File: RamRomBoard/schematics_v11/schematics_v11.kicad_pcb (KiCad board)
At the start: 2 copper layers, 100 x 100 mm, 101 parts, among them J1 BUS, J10 Micro_SD_Card_Det2, J2 BUS, J3 VSEL, J5 Screw_Terminal_01x02, J6 USB_B_Micro, J7 STM32F401, J8 Dual LED Socket, J9 JTAG, SW1 033TBVSA, SW2 SW_Push, U1 74LVC125, U10 74AHC1G14, U11 IS61WV102416FBLL1T2, U12 IS61WV10248EDBLL-10TL, U13 74LVC595, U14 74LVC595, U15 SN74LVC245ANSR, U16 SN74LVC245ANSR, U17 74LVC595, U18 74HC165, U19 SN74LVC245ANSR, U2 AZ1117-3.3, U20 DS1314, U3 74LVC08AD, U4 DS1085, U5 74LVC1G32, U6 74AHC1G14, U7 74HC590, U8 74HC590, U9 74HC590

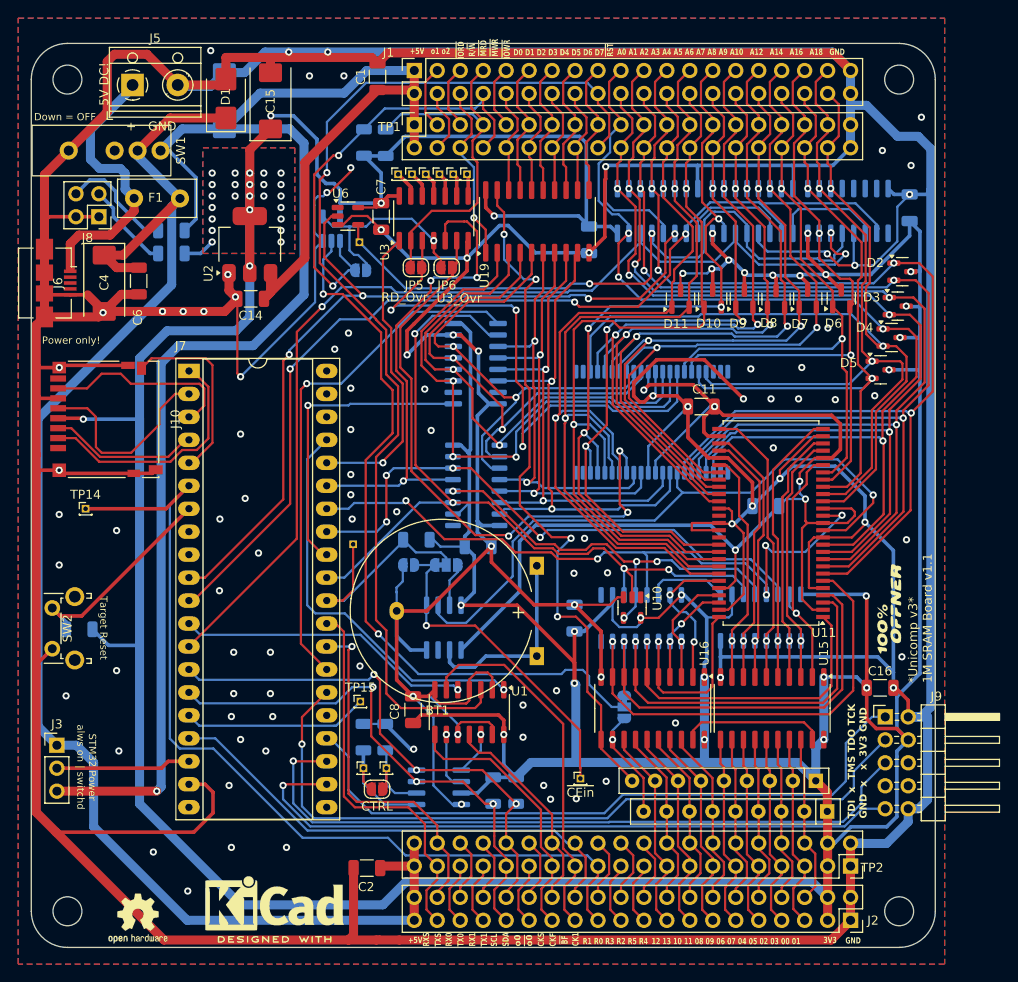
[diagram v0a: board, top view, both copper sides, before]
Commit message: new vhdl code
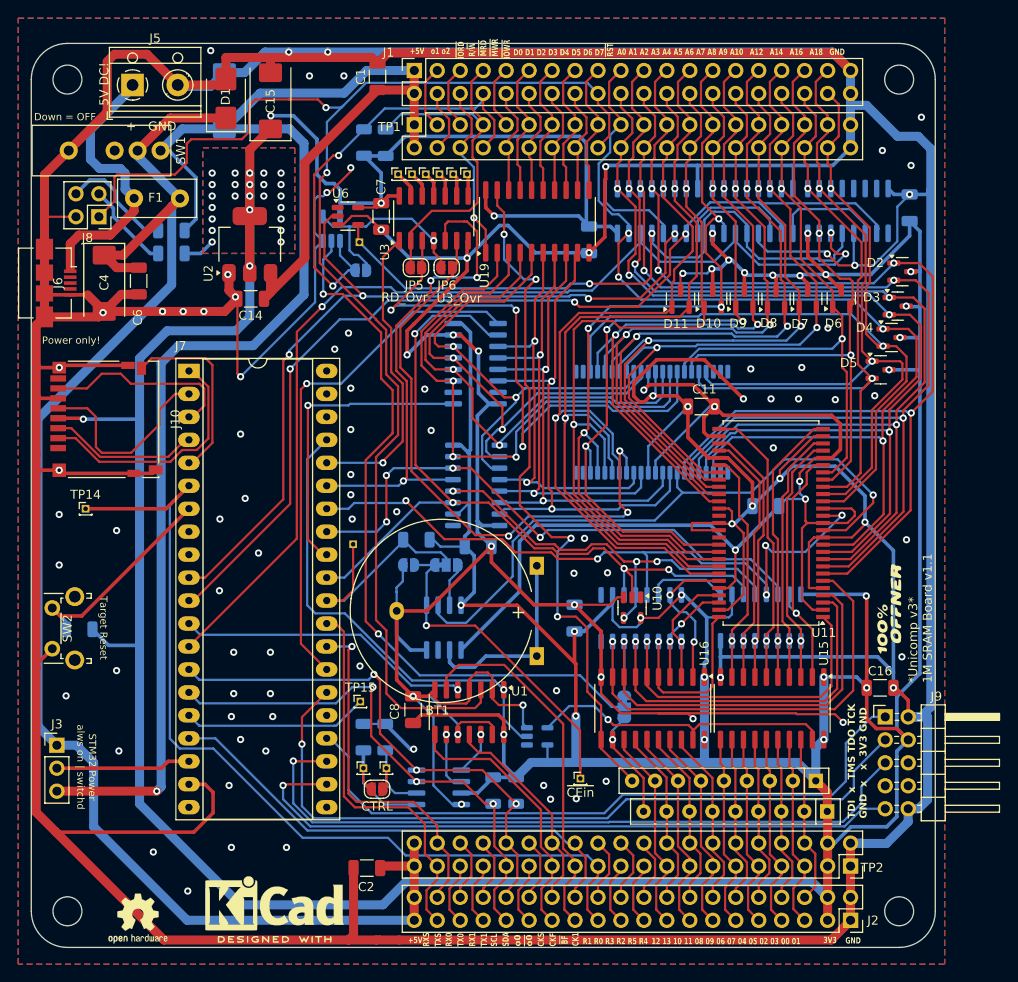
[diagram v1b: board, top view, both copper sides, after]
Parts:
- added U21: 74AHC1G14, Package_TO_SOT_SMD:SOT-23-5, B.Cu at (106.0, 126.7)
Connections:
- J8 pad 1: GND -> /~{RST}
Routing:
- net GND: track 1079.2 -> 1117.9 mm
- net /~{RST}: track 120.7 -> 158.0 mm, vias 1 -> 2
- net /~{CE_EXT_EN}: track 16.0 -> 35.1 mm, vias 0 -> 1
- net /~{TRST}: track 44.8 -> 51.4 mm
- net Net-(JP4-C): track 81.5 -> 80.6 mm

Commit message: graphic updates
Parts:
- added R11: 1k, Resistor_SMD:R_1206_3216Metric, B.Cu at (87.6, 62.0)
- moved R7 4.10 mm to (87.3, 56.9), turned to 0 degrees
- moved R8 2.61 mm to (87.3, 59.2), turned to 0 degrees
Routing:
- net /R/~{W}_e: track 19.9 -> 29.1 mm
- net +3V3: track 664.8 -> 671.4 mm
- net /~{MWR}: track 50.2 -> 53.5 mm
- net /~{RST}: track 158.0 -> 156.6 mm
- net /~{MRD}: track 41.1 -> 41.6 mm
